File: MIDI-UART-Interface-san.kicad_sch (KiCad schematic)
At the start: 33 parts, among them CN1 Conn_01x04_Female, J1 AudioJack3, J2 AudioJack3, J3 Conn_01x03_Female, J4 Conn_01x03_Female, U1 CD74HC4050PWR, U2 TLP2361_TPL_E

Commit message: Update to revision 2
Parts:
- removed J1: AudioJack3, MIDI-UART-Interface-san:3.5mm_Stereo_TRS_PJ-3210-4A_and_ST-005-G, symbol Connector:AudioJack3
- added J1: AudioJack3, MIDI-UART-Interface-san:3.5mm_Stereo_TRS_PJ-3210-4A_and_ST-005-G, symbol Connector_Audio:AudioJack3
- added U3: BAS40DW-04-7-F, MIDI-UART-Interface-san:SOT-363_DIO, symbol BAS70DW-04:BAS70DW-04-7-F
- C1: LCSC C176682 -> C176674
- LED1: LCSC C2286 -> C965799
- U1: value CD74HC4050PWR -> CD74HC4050PWR/74HC4050PW; LCSC C352825 -> C546991
- U2: symbol dk_Optoisolators-Logic-Output:TLP2361_TPL_E -> MIDI-Interface-san-rescue:TLP2361_TPL_E-dk_Optoisolators-Logic-Output; LCSC (none) -> C107626
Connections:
- net C1: now reaches R4.2
- net C1: now also U3.2 (C1), U3.5 (C2)
- net A1: now reaches D1.2 (A), U2.3
- net A1: now also U3.1 (A1), U3.4 (A2)
- new net in_R: J1.R, U3.3 (AC2)
- new net in_T: J1.T, U3.6 (AC1)
- no-connect marks 3 -> 4
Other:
- company: Kinoshita Laboratory -> (none)
- title: MIDI-UART Interface san -> MIDI-UART Interface-san
- moved on the sheet: C1, C3, CN1, D1, J2, J3, J4, LED1, LED2, LED3, R1, R2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
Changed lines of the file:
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@@
-(kicad_sch (version 20211123) (generator eeschema)
-  (paper "A4")
-  (title_block
-    (title "MIDI-UART Interface san")
-    (date "2021-06-09")
-    (company "Kinoshita Laboratory")
-    (comment 1 "drawn by: Kazuki Saita")
-  )
+(kicad_sch
+	(version 20231120)
+	(generator "eeschema")
+	(generator_version "8.0")
+	(paper "A4")
+	(title_block
+		(title "MIDI-UART Interface-san")
+		(date "2021-12-11")
+	)

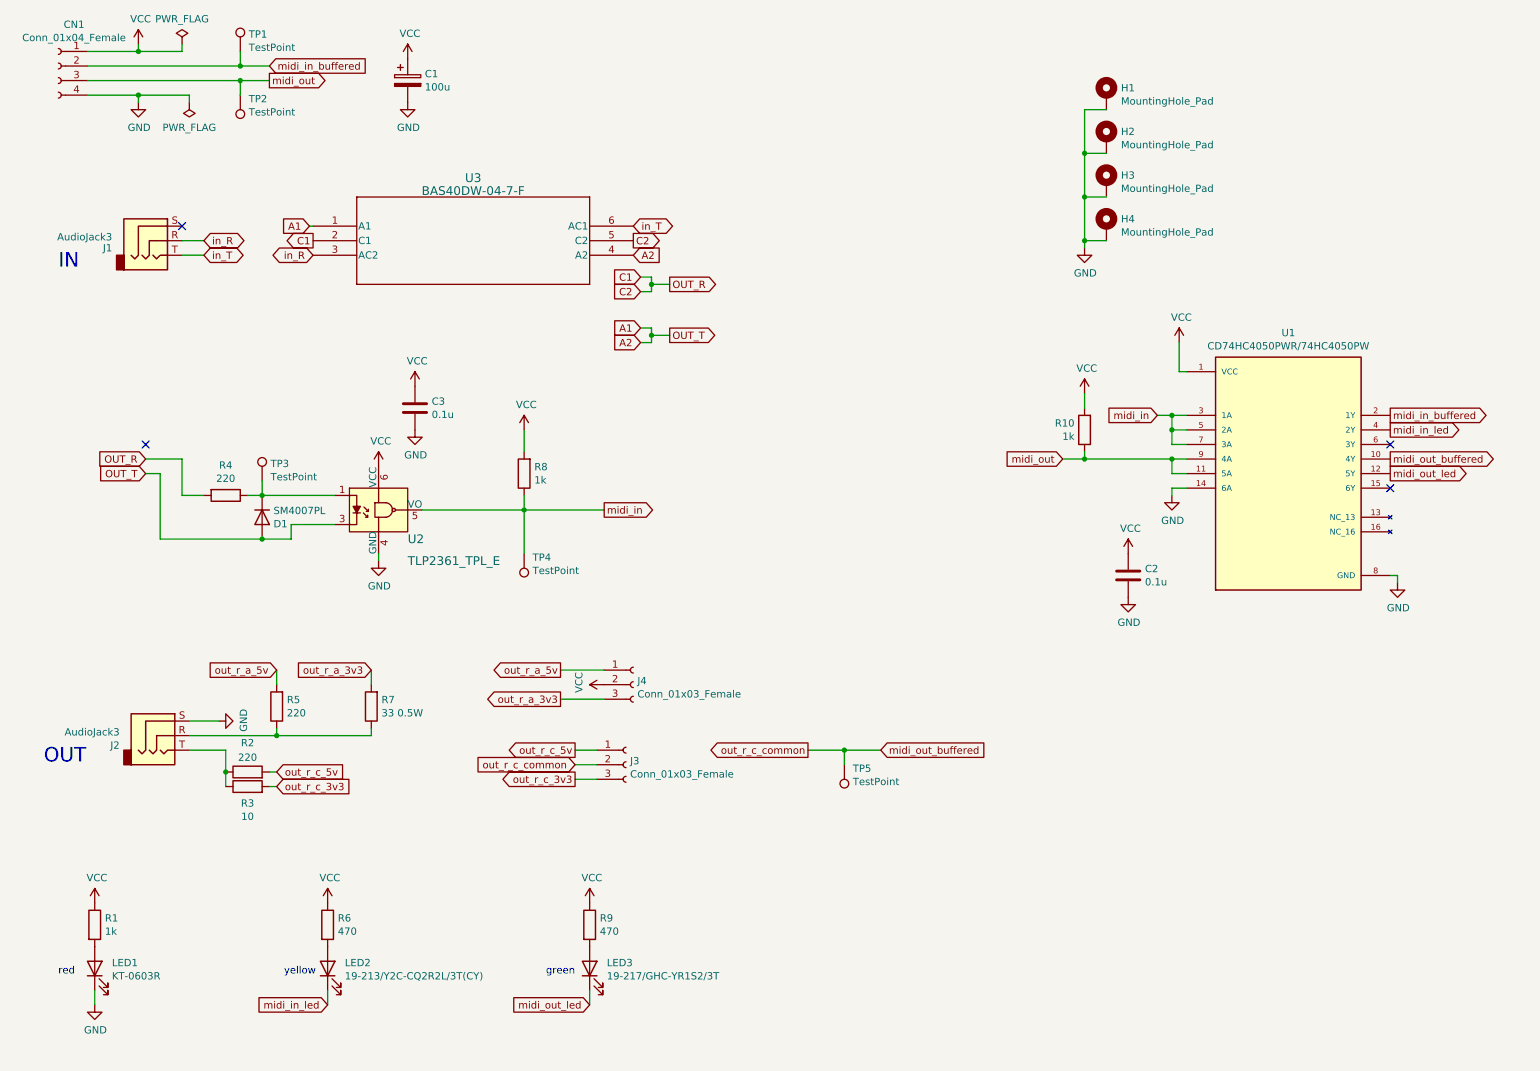
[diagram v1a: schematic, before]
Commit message: Revise to 2.1, KiCad 9.0
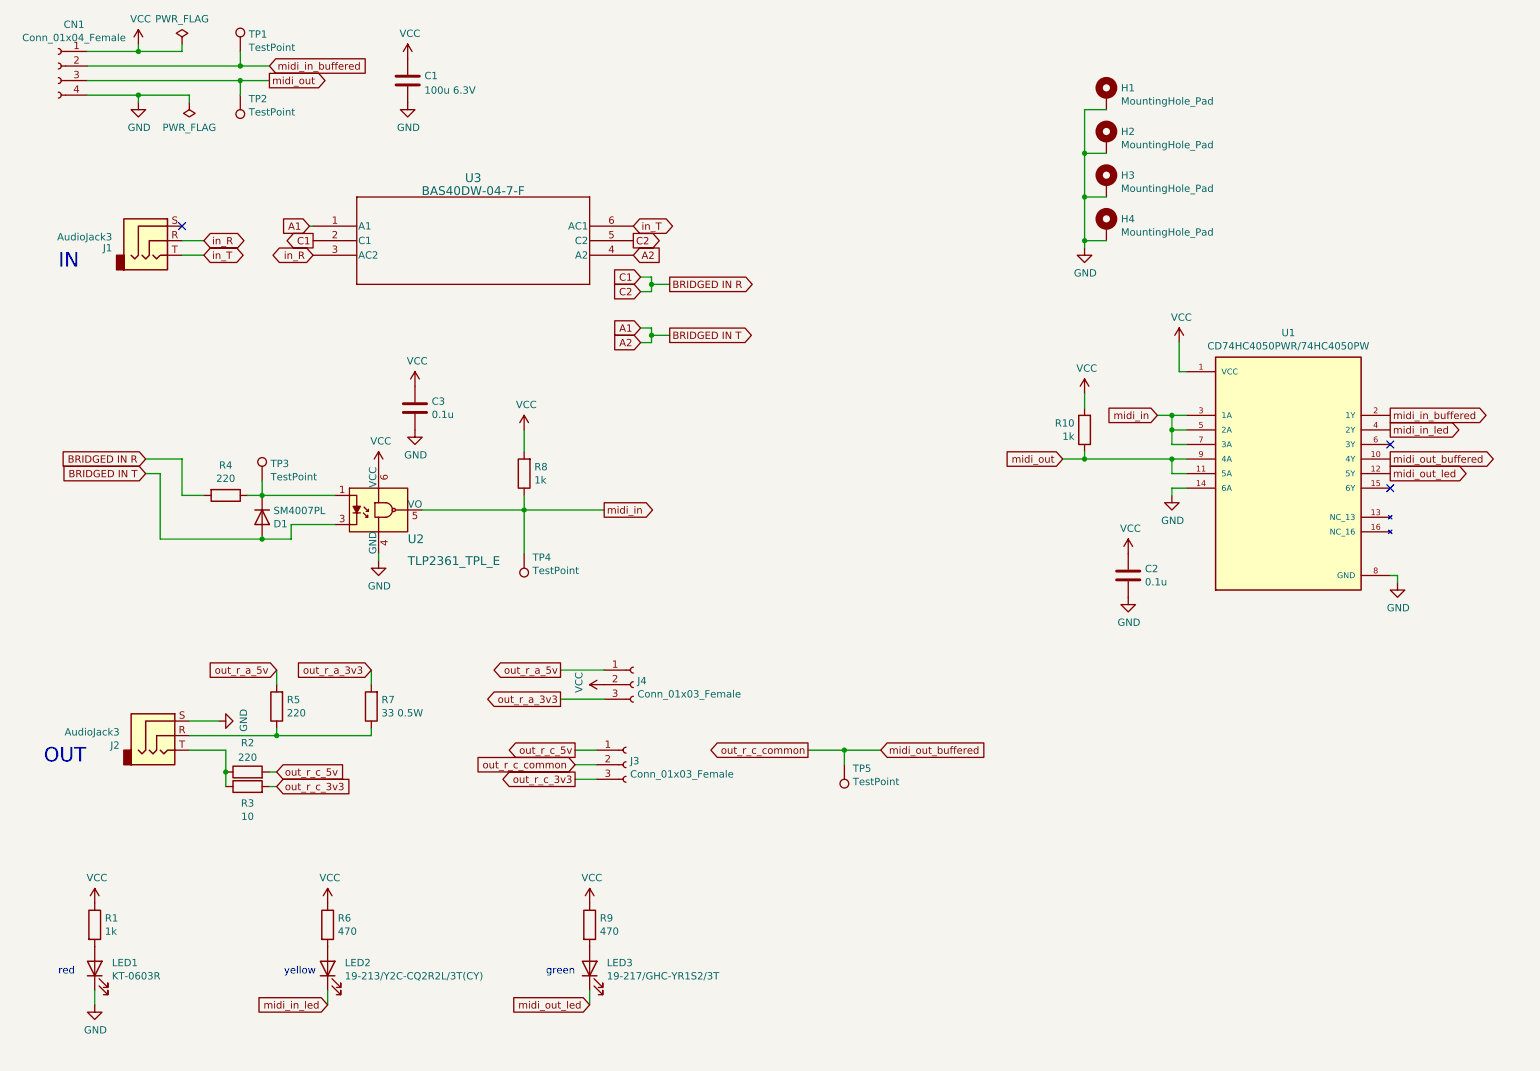
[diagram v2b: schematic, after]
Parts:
- removed C1: 100u, Capacitor_SMD:CP_Elec_6.3x5.3, symbol Device:CP
- added C1: 100u 6.3V, Capacitor_SMD:C_1206_3216Metric_Pad1.33x1.80mm_HandSolder, symbol Device:C
- J1: footprint MIDI-UART-Interface-san:3.5mm_Stereo_TRS_PJ-3210-4A_and_ST-005-G -> my_footprint:3.5mm_Stereo_TRS_PJ-3210-4A_and_ST-005-G
- J2: footprint MIDI-UART-Interface-san:3.5mm_Stereo_TRS_PJ-3210-4A_and_ST-005-G -> MIDI-Interface-san:3.5mm_Stereo_TRS_PJ-3210-4A_and_ST-005-G
- TP1, TP2, TP3, TP4, TP5: footprint MIDI-UART-Interface-san:TP_1PAD -> my_footprint:TP_1PAD
- U1: footprint MIDI-UART-Interface-san:SOP65P640X120-16N -> MIDI-Interface-san:SOP65P640X120-16N
- U3: footprint MIDI-UART-Interface-san:SOT-363_DIO -> ultra_librarian:SOT-363_DIO
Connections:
- net GND: now also C1.2
- net VCC: now also C1.1
- net C1 renamed BRIDGED IN R
- no-connect marks 4 -> 3
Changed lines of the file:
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@@
 (kicad_sch
-	(version 20231120)
+	(version 20250114)
 	(generator "eeschema")
-	(generator_version "8.0")
+	(generator_version "9.0")
 	(paper "A4")
 	(title_block
